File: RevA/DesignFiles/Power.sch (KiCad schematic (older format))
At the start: 15 parts, among them J101 USB_OTG, U1 ICE40HX1K-TQ144, U102 LT3030EFE

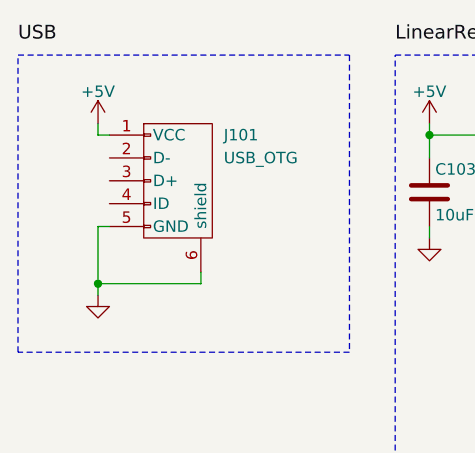
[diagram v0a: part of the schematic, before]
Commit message: placining heirarchy pins
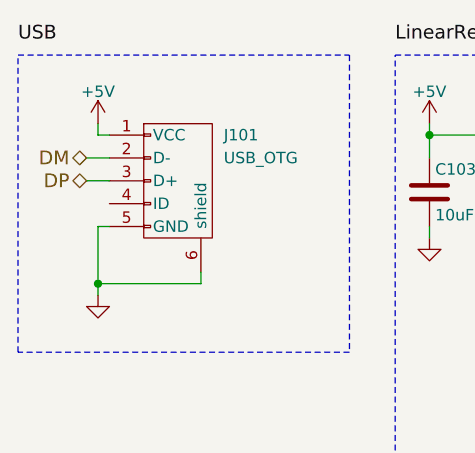
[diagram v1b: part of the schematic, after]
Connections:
- net DM: now reaches J101.2 (D-)
- net DP: now reaches J101.3 (D+)
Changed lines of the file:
@@
 Text Label 6950 600  0    60   ~ 0
 FPGA-Power
+Text HLabel 950  1100 0    60   BiDi ~ 0
+DM
+Text HLabel 950  1200 0    60   BiDi ~ 0
+DP
+Wire Wire Line
+	1050 1200 950  1200
+Wire Wire Line
+	950  1100 1050 1100
 $EndSCHEMATC
